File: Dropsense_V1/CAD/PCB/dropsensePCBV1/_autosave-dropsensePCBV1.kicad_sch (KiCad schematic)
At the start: 26 parts, among them J1 Micro_SD_Card_Det_Hirose_DM3AT, J2 USB_B_Micro, J3 Conn_01x02_Socket, SW1 SW_Push, SW2 SW_Push, U1 ESP32-S3-WROOM-1, U2 MPU-6050, U3 TP4056-42-ESOP8, U4 ME6211C10M5

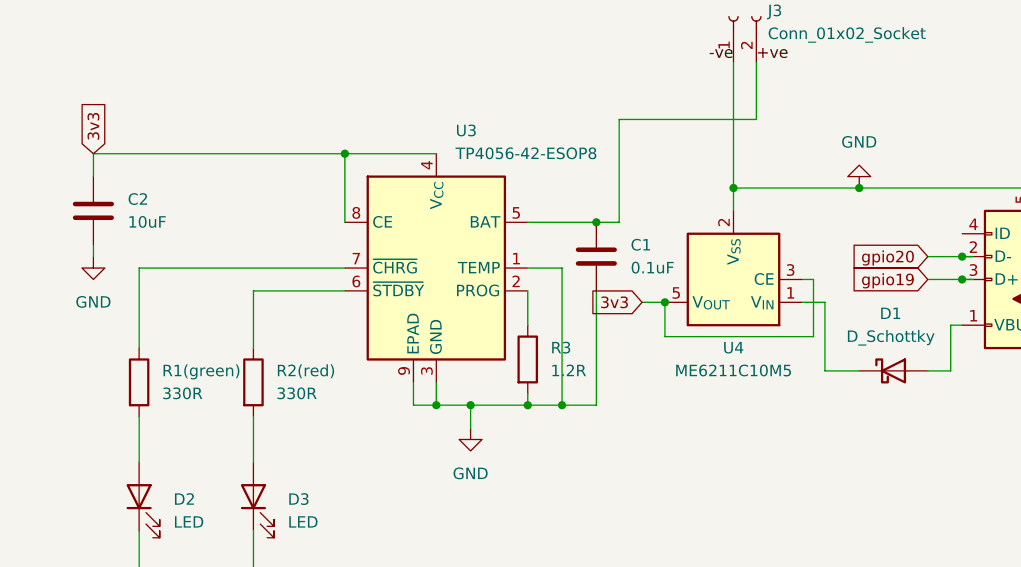
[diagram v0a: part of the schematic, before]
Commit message: STARTED PCB SCHEMATICS WORK
started pcb schematics work and finished the schematics
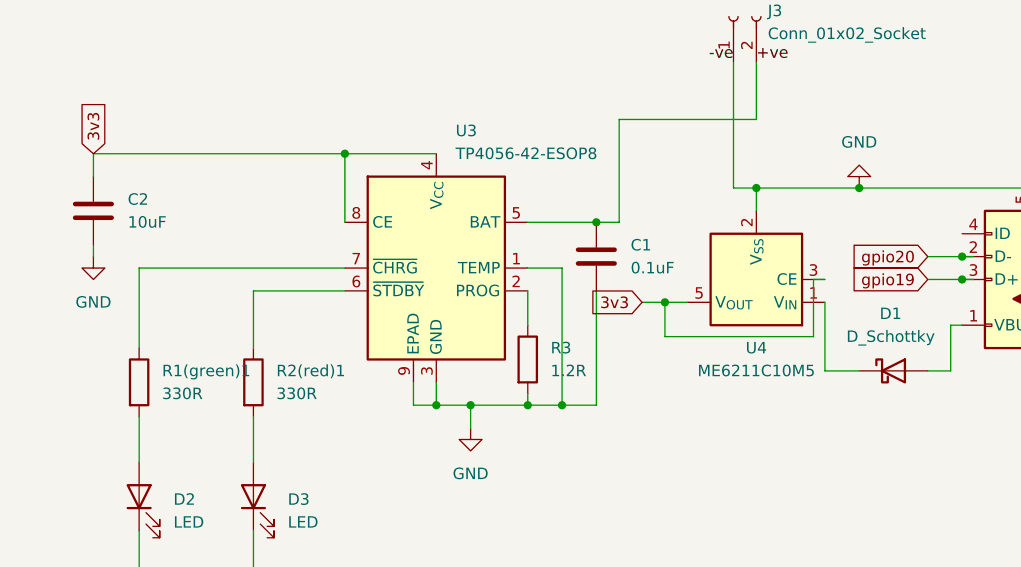
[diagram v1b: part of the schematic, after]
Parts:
- J3: footprint Connector_JST:JST_ACH_BM01B-ACHSS-A-GAN-ETF_1x01-1MP_P1.20mm_Vertical -> Connector_PinHeader_2.54mm:PinHeader_1x02_P2.54mm_Vertical
- renumbered R1(green) to R1(green)1, R2(red) to R2(red)1
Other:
- moved on the sheet: U4
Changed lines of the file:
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@@
+	)
+	(junction
+		(at 241.3 41.91)
+		(diameter 0)
+		(color 0 0 0 0)
 	)
 	(junction
@@
 		(color 0 0 0 0)
 	)
-	(junction
-		(at 238.76 41.91)
-		(diameter 0)
-		(color 0 0 0 0)
-	)
 	(bus_entry
 		(at 107.95 49.53)
@@
 	(wire
 		(pts
+			(xy 241.3 41.91) (xy 238.76 41.91)
+		)
+		(stroke
+			(width 0)
+			(type default)
+		)
+	)
+	(wire
+		(pts
 			(xy 219.71 66.04) (xy 223.52 66.04)
 		)
@@
 	(wire
 		(pts
-			(xy 246.38 54.61) (xy 248.92 54.61)
-		)
-		(stroke
-			(width 0)
-			(type default)
-		)
-	)
-	(wire
-		(pts
 			(xy 205.74 63.5) (xy 205.74 66.04)
 		)
@@
 	(wire
 		(pts
-			(xy 238.76 41.91) (xy 238.76 44.45)
+			(xy 241.3 41.91) (xy 241.3 44.45)
 		)
 		(stroke
@@
 	(wire
 		(pts
+			(xy 233.68 54.61) (xy 231.14 54.61)
+		)
+		(stroke
+			(width 0)
+			(type default)
+		)
+	)
+	(wire
+		(pts
 			(xy 203.2 66.04) (xy 205.74 66.04)
 		)
@@
 	(wire
 		(pts
-			(xy 246.38 52.07) (xy 247.65 52.07)
+			(xy 248.92 52.07) (xy 247.65 52.07)
 		)
 		(stroke
@@
 	(wire
 		(pts
-			(xy 252.73 41.91) (xy 238.76 41.91)
+			(xy 252.73 41.91) (xy 241.3 41.91)
 		)
 		(stroke
@@
 		(dnp no)
 		(fields_autoplaced yes)
-		(property "Reference" "R2(red)"
+		(property "Reference" "R2(red)1"
 			(at 187.96 62.2299 0)
 			(effects
@@
 			(project "dropsensePCBV1"
 				(path "/69b1a30b-982d-40a0-b848-7776f317f216"
-					(reference "R2(red)")
+					(reference "R2(red)1")
 					(unit 1)
 				)
@@
 	(symbol
 		(lib_id "Regulator_Linear:ME6211C10M5")
-		(at 238.76 52.07 180)
+		(at 241.3 52.07 180)
 		(unit 1)
 		(exclude_from_sim no)
@@
 		(fields_autoplaced yes)
 		(property "Reference" "U4"
-			(at 238.76 59.69 0)
+			(at 241.3 59.69 0)
 			(effects
 				(font
@@
 		)
 		(property "Value" "ME6211C10M5"
-			(at 238.76 62.23 0)
+			(at 241.3 62.23 0)
 			(effects
 				(font
@@
 		)
 		(property "Footprint" "Package_TO_SOT_SMD:SOT-23-5"
-			(at 239.268 38.608 0)
+			(at 241.808 38.608 0)
 			(effects
 				(font
@@
 		)
 		(property "Datasheet" "https://www.lcsc.com/datasheet/lcsc_datasheet_2304140030_MICRONE-Nanjing-Micro-One-Elec-ME6211C33R5G_C235316.pdf"
-			(at 238.506 35.052 0)
+			(at 241.046 35.052 0)
 			(effects
 				(font
@@
 		)
 		(property "Description" "300mA low dropout linear regulator, shutdown pin, 6.5V max input voltage, 1.0V fixed positive output, SOT-23-5"
-			(at 236.982 36.83 0)
+			(at 239.522 36.83 0)
 			(effects
 				(font
@@
 			)
 		)
-		(property "Footprint" "Connector_JST:JST_ACH_BM01B-ACHSS-A-GAN-ETF_1x01-1MP_P1.20mm_Vertical"
+		(property "Footprint" "Connector_PinHeader_2.54mm:PinHeader_1x02_P2.54mm_Vertical"
 			(at 238.76 22.86 0)
 			(effects
@@
 		(dnp no)
 		(fields_autoplaced yes)
-		(property "Reference" "R1(green)"
+		(property "Reference" "R1(green)1"
 			(at 175.26 62.2299 0)
 			(effects
@@
 			(project ""
 				(path "/69b1a30b-982d-40a0-b848-7776f317f216"
-					(reference "R1(green)")
+					(reference "R1(green)1")
 					(unit 1)
 				)
